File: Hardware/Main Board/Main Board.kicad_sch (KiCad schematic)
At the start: 67 parts, among them J1 Micro_SD_Card_Det1, J2 Camera Module, J3 Conn_01x09_Socket, J4 MIC 1 Connector, J5 MIC 2 Connector, J6 USB_C_Receptacle_USB2.0_16P, J7 OLED, Q1 AO3401A, U1 ESP32-S3-WROOM-2, U2 TPS63060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

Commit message: received feedback from Andy + others and revised board
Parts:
- added H3, H4: MountingHole, MountingHole:MountingHole_2.1mm, symbol Mechanical:MountingHole
- added TP7, TP8: TestPoint, TestPoint:TestPoint_Pad_1.0x1.0mm, symbol Connector:TestPoint
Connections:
- net D+: now also TP7.1
- net D-: now also TP8.1

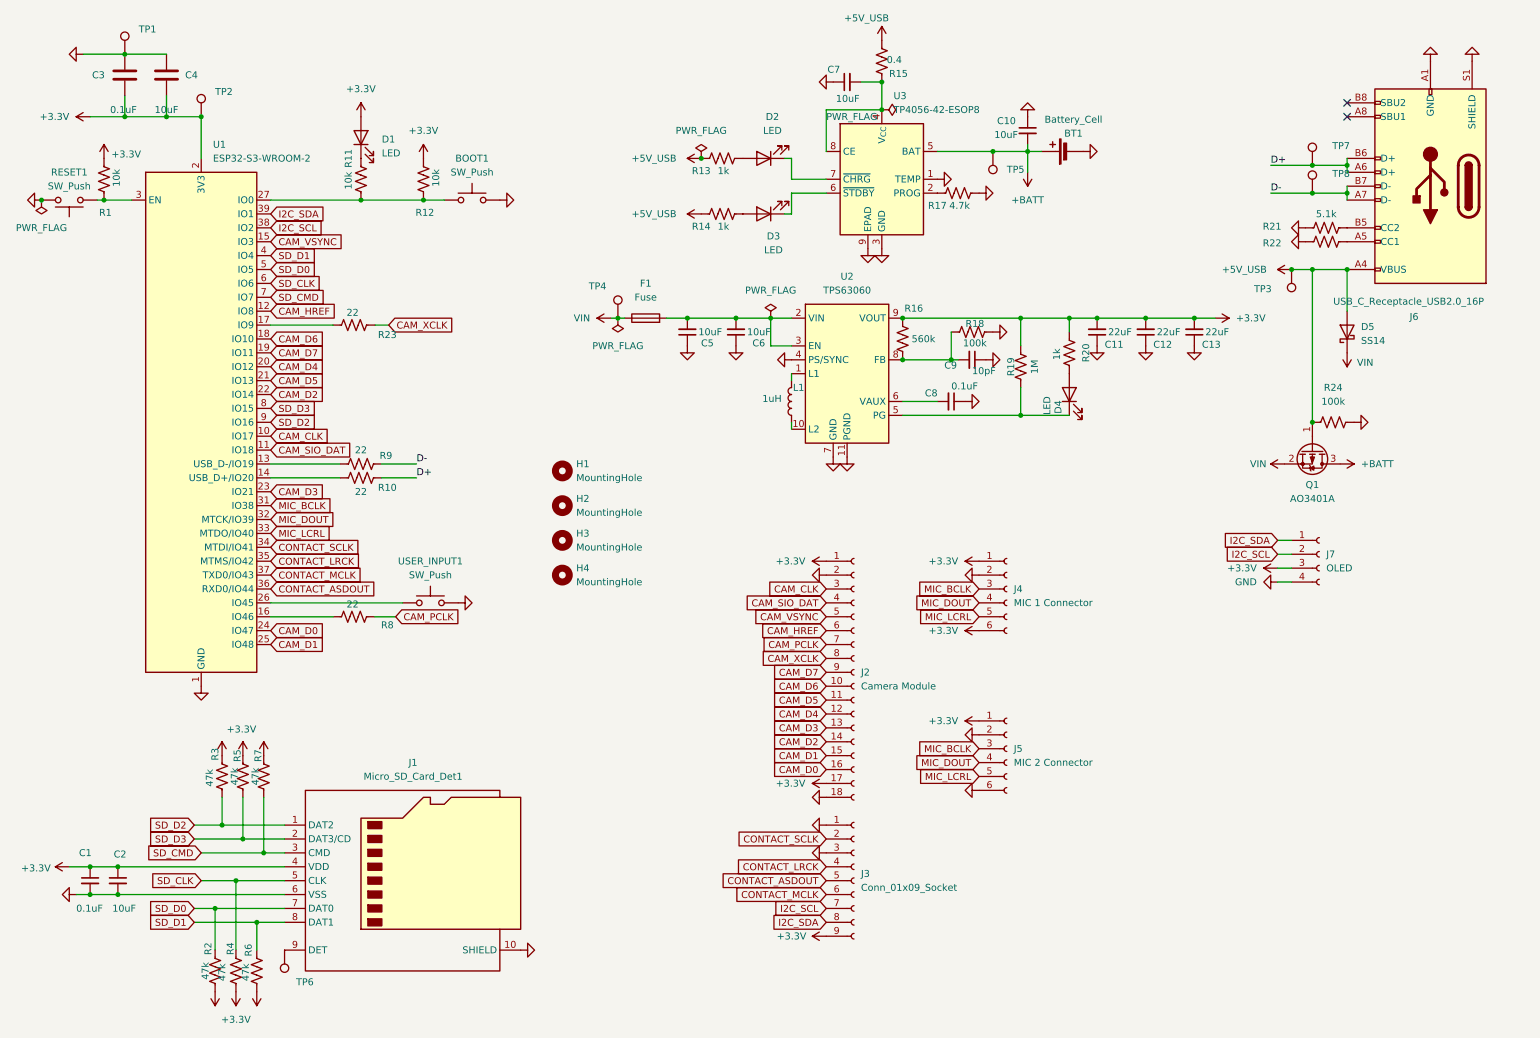
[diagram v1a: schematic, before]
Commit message: submitted for manufacturinng. Flipped contact mic connections on main board to be aligned with contact mic board
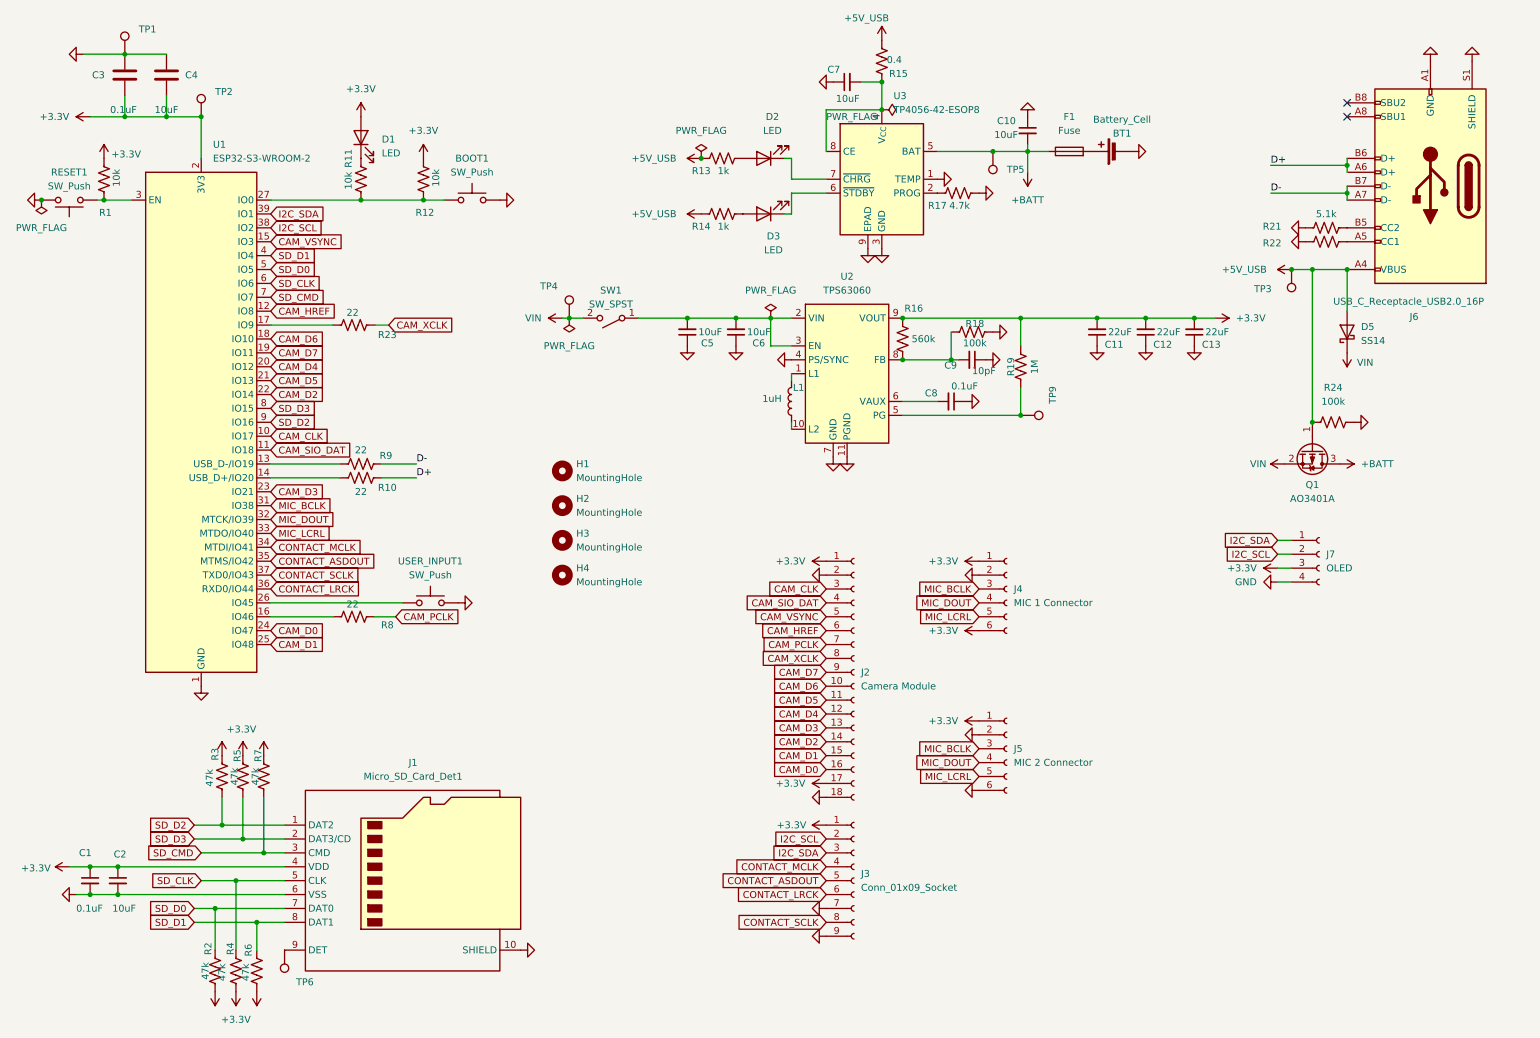
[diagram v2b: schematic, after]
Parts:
- removed D4: LED, LED_SMD:LED_0603_1608Metric, symbol Device:LED
- removed R20: 1k, Resistor_SMD:R_0402_1005Metric, symbol Device:R_US
- removed TP7, TP8: TestPoint, TestPoint:TestPoint_Pad_1.0x1.0mm, symbol Connector:TestPoint
- added SW1: SW_SPST, Button_Switch_SMD:SW_SPDT_PCM12, symbol Switch:SW_SPST
- added TP9: TestPoint, TestPoint:TestPoint_Pad_1.0x1.0mm, symbol Connector:TestPoint
- BT1: footprint Connector_JST:JST_GH_SM02B-GHS-TB_1x02-1MP_P1.25mm_Horizontal -> Connector_JST:JST_PH_S2B-PH-K_1x02_P2.00mm_Horizontal
- D1: footprint LED_SMD:LED_0603_1608Metric -> Connector_PinHeader_2.00mm:PinHeader_1x02_P2.00mm_Vertical
- USER_INPUT1: footprint Button_Switch_SMD:SW_SPST_PTS645 -> Button_Switch_SMD:SW_SPST_TL3342
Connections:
- net +3.3V: now also J3.1 (Pin_1); no longer J3.9 (Pin_9)
- net +BATT: now also F1.1; no longer BT1.1 (+)
- net CONTACT_ASDOUT: now also U1.35 (MTMS/IO42); no longer U1.36 (RXD0/IO44)
- net CONTACT_LRCK: now also J3.6 (Pin_6), U1.36 (RXD0/IO44); no longer J3.4 (Pin_4), U1.35 (MTMS/IO42)
- net CONTACT_MCLK: now also J3.4 (Pin_4), U1.34 (MTDI/IO41); no longer J3.6 (Pin_6), U1.37 (TXD0/IO43)
- net CONTACT_SCLK: now also J3.8 (Pin_8), U1.37 (TXD0/IO43); no longer J3.2 (Pin_2), U1.34 (MTDI/IO41)
- net GND: now also J3.7 (Pin_7), J3.9 (Pin_9); no longer J3.1 (Pin_1), J3.3 (Pin_3)
- net I2C_SCL: now also J3.2 (Pin_2); no longer J3.7 (Pin_7)
- net I2C_SDA: now also J3.3 (Pin_3); no longer J3.8 (Pin_8)
- net VIN: now also SW1.2 (B); no longer F1.1
- net at R19.1, U2.5 (PG): now also TP9.1
- net at C5.2, C6.2, U2.2 (VIN)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: now also SW1.1 (A); no longer F1.2
- new net: BT1.1 (+), F1.2
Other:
- moved on the sheet: BT1, F1, TP4

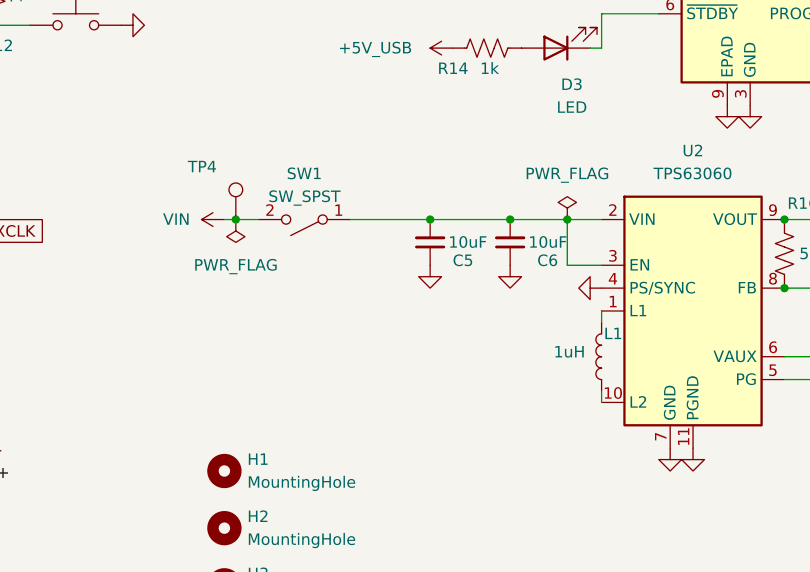
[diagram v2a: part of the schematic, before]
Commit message: fixed power button and via proximity to pad on main board
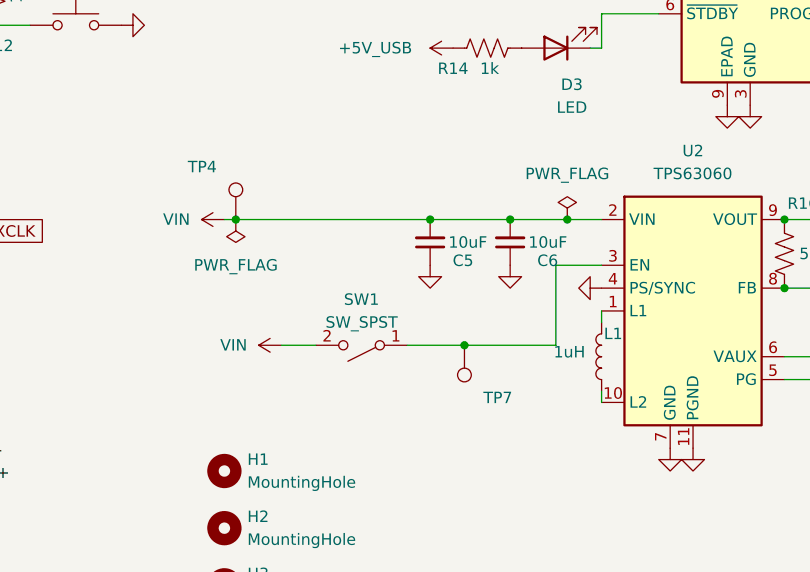
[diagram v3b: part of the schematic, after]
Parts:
- added TP7: TestPoint, TestPoint:TestPoint_Pad_1.0x1.0mm, symbol Connector:TestPoint
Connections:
- net VIN: now also C5.2, C6.2, U2.2 (VIN)
- new net: SW1.1 (A), TP7.1, U2.3 (EN)
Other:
- moved on the sheet: SW1
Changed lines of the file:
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@@
 	)
 	(junction
+		(at 139.7 82.55)
+		(diameter 0)
+		(color 0 0 0 0)
+	)
+	(junction
 		(at 29.21 46.99)
 		(diameter 0)
@@
 	(wire
 		(pts
+			(xy 114.3 68.58) (xy 135.89 68.58)
+		)
+		(stroke
+			(width 0)
+			(type default)
+		)
+	)
+	(wire
+		(pts
 			(xy 171.45 25.4) (xy 171.45 30.48)
 		)
@@
 	(wire
 		(pts
-			(xy 198.12 36.83) (xy 198.12 38.1)
+			(xy 119.38 82.55) (xy 123.19 82.55)
 		)
 		(stroke
@@
 	(wire
 		(pts
-			(xy 127 68.58) (xy 135.89 68.58)
+			(xy 198.12 36.83) (xy 198.12 38.1)
 		)
 		(stroke
@@
 	(wire
 		(pts
-			(xy 250.19 59.69) (xy 250.19 87.63)
+			(xy 133.35 82.55) (xy 139.7 82.55)
 		)
 		(stroke
@@
 	(wire
 		(pts
-			(xy 71.12 69.85) (xy 59.69 69.85)
+			(xy 250.19 59.69) (xy 250.19 87.63)
 		)
 		(stroke
@@
 	(wire
 		(pts
-			(xy 114.3 68.58) (xy 116.84 68.58)
+			(xy 71.12 69.85) (xy 59.69 69.85)
 		)
 		(stroke
@@
 	(wire
 		(pts
-			(xy 151.13 73.66) (xy 154.94 73.66)
+			(xy 149.86 73.66) (xy 154.94 73.66)
 		)
 		(stroke
@@
 	(wire
 		(pts
-			(xy 151.13 68.58) (xy 151.13 73.66)
+			(xy 22.86 168.91) (xy 26.67 168.91)
 		)
 		(stroke
@@
 	(wire
 		(pts
-			(xy 22.86 168.91) (xy 26.67 168.91)
+			(xy 87.63 46.99) (xy 91.44 46.99)
 		)
 		(stroke
@@
 	(wire
 		(pts
-			(xy 87.63 46.99) (xy 91.44 46.99)
+			(xy 256.54 45.72) (xy 256.54 46.99)
 		)
 		(stroke
@@
 	(wire
 		(pts
-			(xy 256.54 45.72) (xy 256.54 46.99)
+			(xy 33.02 27.94) (xy 33.02 31.75)
 		)
 		(stroke
@@
 	(wire
 		(pts
-			(xy 33.02 27.94) (xy 33.02 31.75)
+			(xy 191.77 38.1) (xy 198.12 38.1)
 		)
 		(stroke
@@
 	(wire
 		(pts
-			(xy 191.77 38.1) (xy 198.12 38.1)
+			(xy 256.54 39.37) (xy 256.54 40.64)
 		)
 		(stroke
@@
 	(wire
 		(pts
-			(xy 256.54 39.37) (xy 256.54 40.64)
+			(xy 154.94 49.53) (xy 154.94 45.72)
 		)
 		(stroke
@@
 	(wire
 		(pts
-			(xy 154.94 49.53) (xy 154.94 45.72)
+			(xy 149.86 73.66) (xy 149.86 82.55)
 		)
 		(stroke
@@
 	(wire
 		(pts
+			(xy 139.7 82.55) (xy 149.86 82.55)
+		)
+		(stroke
+			(width 0)
+			(type default)
+		)
+	)
+	(wire
+		(pts
 			(xy 256.54 44.45) (xy 256.54 45.72)
 		)
@@
 	(symbol
 		(lib_id "Switch:SW_SPST")
-		(at 121.92 68.58 180)
+		(at 128.27 82.55 180)
 		(unit 1)
 		(exclude_from_sim no)
@@
 		(fields_autoplaced yes)
 		(property "Reference" "SW1"
-			(at 121.92 63.5 0)
+			(at 128.27 77.47 0)
 			(effects
 				(font
@@
 		)
 		(property "Value" "SW_SPST"
-			(at 121.92 66.04 0)
+			(at 128.27 80.01 0)
 			(effects
 				(font
@@
 		)
 		(property "Footprint" "Button_Switch_SMD:SW_SPDT_PCM12"
-			(at 121.92 68.58 0)
+			(at 128.27 82.55 0)
 			(effects
 				(font
@@
 		)
 		(property "Datasheet" "~"
-			(at 121.92 68.58 0)
+			(at 128.27 82.55 0)
 			(effects
 				(font
@@
 		)
 		(property "Description" "Single Pole Single Throw (SPST) switch"
-			(at 121.92 68.58 0)
+			(at 128.27 82.55 0)
 			(effects
 				(font
@@
 	)
 	(symbol
+		(lib_id "Connector:TestPoint")
+		(at 139.7 82.55 180)
+		(unit 1)
+		(exclude_from_sim no)
+		(in_bom yes)
+		(on_board yes)
+		(dnp no)
+		(property "Reference" "TP7"
+			(at 145.034 88.392 0)
+			(effects
+				(font
+					(size 1.27 1.27)
+				)
+				(justify left)
+			)
+		)
+		(property "Value" "TestPoint"
+			(at 137.16 84.5821 0)
+			(effects
+				(font
+					(size 1.27 1.27)
+				)
+				(justify left)
+				(hide yes)
+			)
+		)
+		(property "Footprint" "TestPoint:TestPoint_Pad_1.0x1.0mm"
+			(at 134.62 82.55 0)
+			(effects
+				(font
+					(size 1.27 1.27)
+				)
+				(hide yes)
+			)
+		)
+		(property "Datasheet" "~"
+			(at 134.62 82.55 0)
+			(effects
+				(font
+					(size 1.27 1.27)
+				)
+				(hide yes)
+			)
+		)
+		(property "Description" "test point"
+			(at 139.7 82.55 0)
+			(effects
+				(font
+					(size 1.27 1.27)
+				)
+				(hide yes)
+			)
+		)
+		(pin "1"
+		)
+		(instances
+			(project "Main Board"
+				(path "/06300a21-1646-41b0-b473-1c39557d6dab"
+					(reference "TP7")
+					(unit 1)
+				)
+			)
+		)
+	)
+	(symbol
 		(lib_id "Device:R_US")
 		(at 142.24 49.53 270)
@@
 					(unit 1)
 				)
+			)
+		)
+	)
+	(symbol
+		(lib_id "power:+BATT")
+		(at 119.38 82.55 90)
+		(unit 1)
+		(exclude_from_sim no)
+		(in_bom yes)
+		(on_board yes)
+		(dnp no)
+		(fields_autoplaced yes)
+		(property "Reference" "#PWR067"
+			(at 123.19 82.55 0)
+			(effects
+				(font
+					(size 1.27 1.27)
+				)
+				(hide yes)
+			)
+		)
+		(property "Value" "VIN"
+			(at 115.57 82.5499 90)
+			(effects
+				(font
+					(size 1.27 1.27)
+				)
+				(justify left)
+			)
+		)
+		(property "Footprint" ""
+			(at 119.38 82.55 0)
+			(effects
+				(font
+					(size 1.27 1.27)
+				)
+				(hide yes)
+			)
+		)
+		(property "Datasheet" ""
+			(at 119.38 82.55 0)
+			(effects
+				(font
+					(size 1.27 1.27)
+				)
+				(hide yes)
+			)
+		)
+		(property "Description" "Power symbol creates a global label with name \"+BATT\""
+			(at 119.38 82.55 0)
+			(effects
+				(font
+					(size 1.27 1.27)
+				)
+				(hide yes)
+			)
+		)
+		(pin "1"
+		)
+		(instances
+			(project "Main Board"
+				(path "/06300a21-1646-41b0-b473-1c39557d6dab"
+					(reference "#PWR067")
+					(unit 1)
+				)

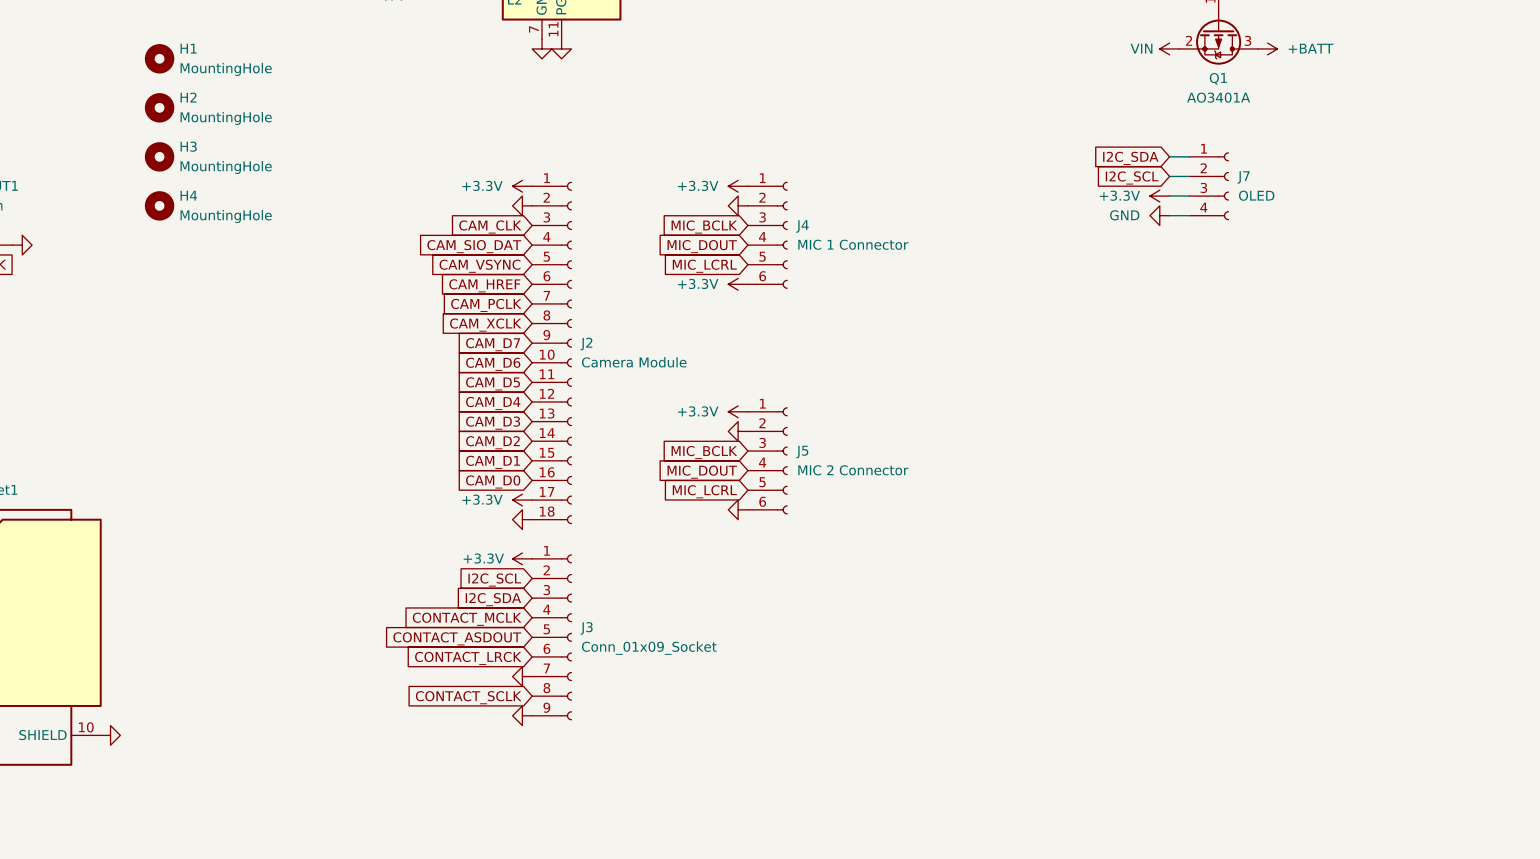
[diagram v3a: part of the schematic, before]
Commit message: began board migration to newer integrated camera 24 pin connector, NOT FINISHED
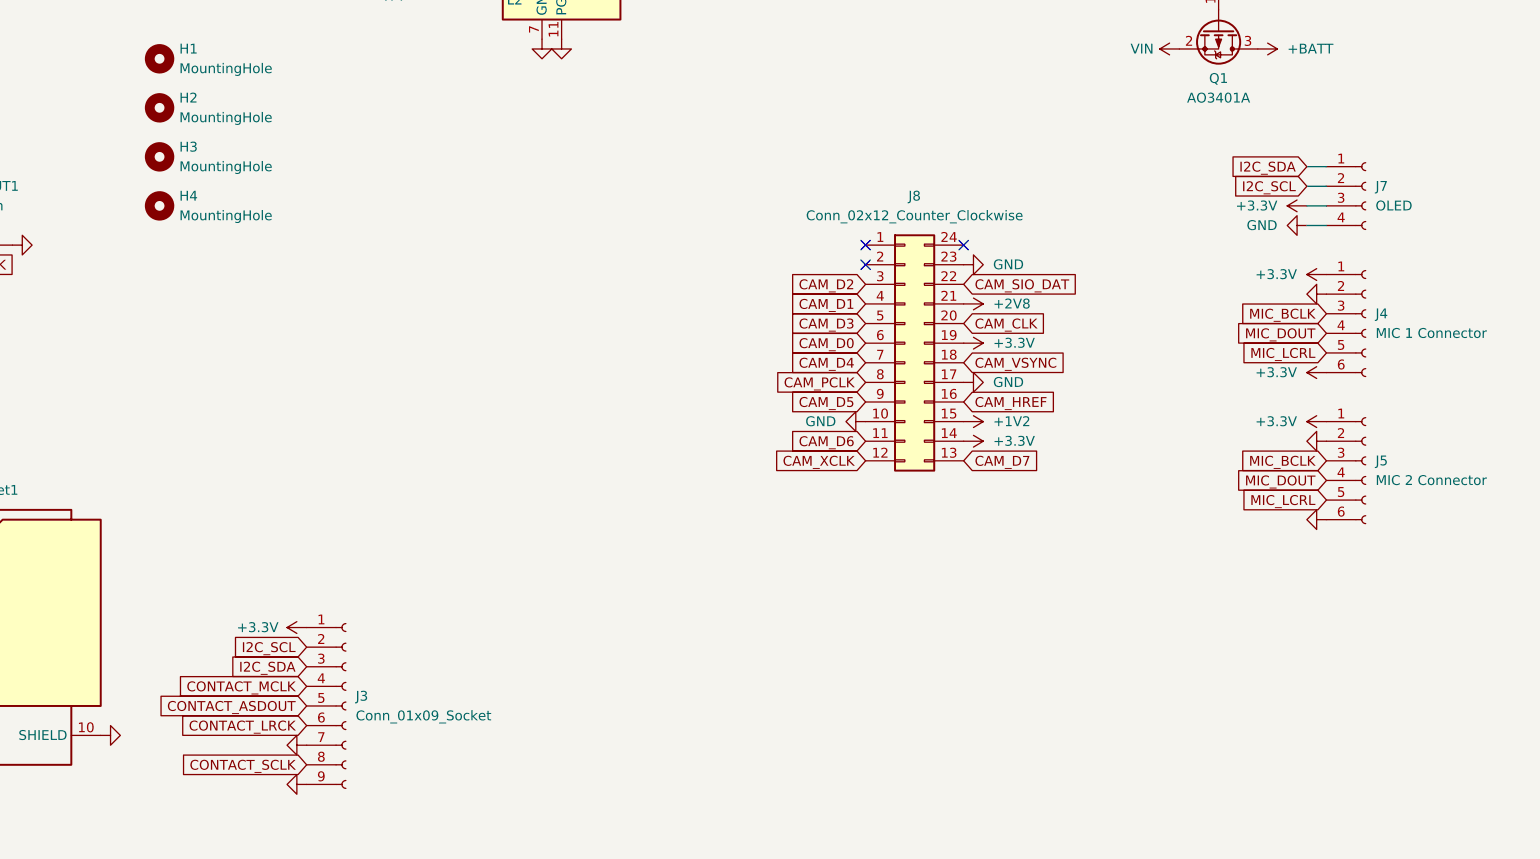
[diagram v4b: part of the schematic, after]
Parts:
- removed J2: Camera Module, Connector_PinHeader_2.54mm:PinHeader_2x09_P2.54mm_Vertical, symbol Connector:Conn_01x18_Socket
- added J8: Conn_02x12_Counter_Clockwise, Connector_FFC-FPC:Hirose_FH12-24S-0.5SH_1x24-1MP_P0.50mm_Horizontal, symbol Connector_Generic:Conn_02x12_Counter_Clockwise
- SW1: footprint Button_Switch_SMD:SW_SPDT_PCM12 -> Connector_PinHeader_2.54mm:PinHeader_1x03_P2.54mm_Vertical
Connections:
- net +3.3V: now also J8.14 (Pin_14), J8.19 (Pin_19)
- net CAM_CLK: now also J8.20 (Pin_20)
- net CAM_D0: now also J8.6 (Pin_6)
- net CAM_D1: now also J8.4 (Pin_4)
- net CAM_D2: now also J8.3 (Pin_3)
- net CAM_D3: now also J8.5 (Pin_5)
- net CAM_D4: now also J8.7 (Pin_7)
- net CAM_D5: now also J8.9 (Pin_9)
- net CAM_D6: now also J8.11 (Pin_11)
- net CAM_D7: now also J8.13 (Pin_13)
- net CAM_HREF: now also J8.16 (Pin_16)
- net CAM_PCLK: now also J8.8 (Pin_8)
- net CAM_SIO_DAT: now also J8.22 (Pin_22)
- net CAM_VSYNC: now also J8.18 (Pin_18)
- net CAM_XCLK: now also J8.12 (Pin_12)
- net GND: now also J8.10 (Pin_10), J8.17 (Pin_17), J8.23 (Pin_23)
- new net +1V2: J8.15 (Pin_15)
- new net +2V8: J8.21 (Pin_21)
- no-connect marks 2 -> 5
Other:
- moved on the sheet: J3, J4, J5, J7
